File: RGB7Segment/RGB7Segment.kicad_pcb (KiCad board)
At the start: 2 copper layers, 18.3 x 17 mm, 21 parts, among them J1 Conn_01x02_Socket, J2 Conn_01x02_Socket

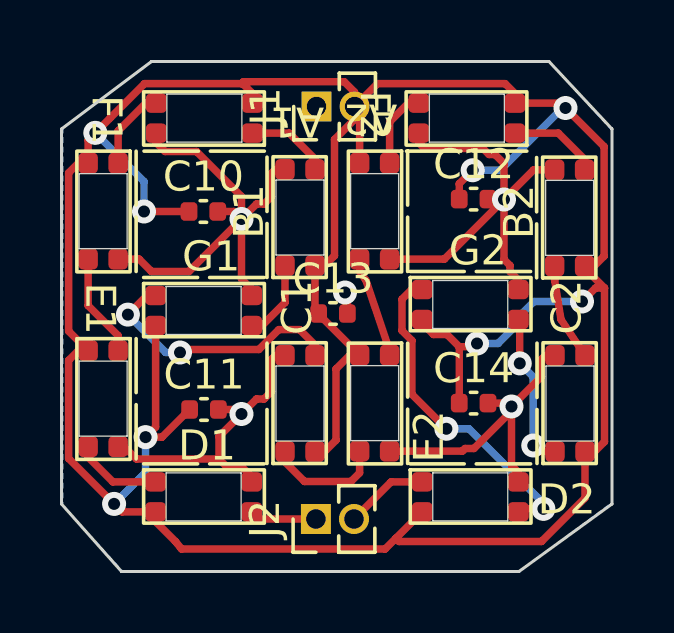
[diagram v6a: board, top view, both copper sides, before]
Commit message: Smaller Footprint, removed all traces, pre-re-layout
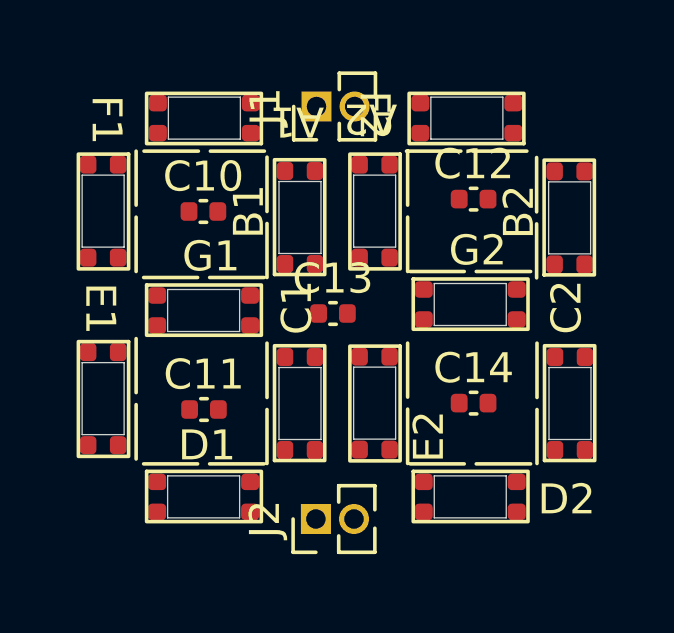
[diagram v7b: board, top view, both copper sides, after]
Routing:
- net VCC: track 109.8 -> 0.50 mm, vias 8 -> 0
- net GND: track 52.9 -> 0.00 mm, vias 5 -> 0
- net Net-(D2-DIN): track 11.1 -> 0.00 mm, vias 2 -> 0
- net Net-(C1-DIN): track 8.83 -> 0.00 mm, vias 2 -> 0
- net Net-(C2-DOUT): track 5.21 -> 0.00 mm, vias 2 -> 0
- net /E2: track 3.95 -> 0.00 mm
- net Net-(E1-DOUT): track 3.46 -> 0.00 mm
- net Net-(E2-DOUT): track 3.42 -> 0.00 mm
- net Net-(B2-DOUT): track 3.25 -> 0.00 mm
- net Net-(A2-DOUT): track 3.04 -> 0.00 mm
- net Net-(D1-DOUT): track 2.94 -> 0.00 mm
- net Net-(A1-DOUT): track 2.79 -> 0.00 mm
- net /DOUT: track 2.79 -> 0.00 mm
- net Net-(A1-DIN): track 2.73 -> 0.00 mm
- net Net-(B1-DOUT): track 2.67 -> 0.00 mm
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- removed copper zone on B.Cu, net GND
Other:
- board size 18.3 x 17 mm -> 1.4 x 2.4 mm

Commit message: New Layout possibility
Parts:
- moved C2 1.28 mm to (208.9, 87.7)
- moved B2 1.27 mm to (208.9, 81.5)
- moved F1 1.12 mm to (194.8, 78.7)
- moved E1 1.11 mm to (194.8, 84.9)
- moved C12 1.00 mm to (205.6, 80.0)
- moved C14 0.65 mm to (205.8, 86.2)
- moved G2 0.60 mm to (204.5, 83.8)
- moved A2 0.56 mm to (207.1, 76.4)
- moved D2 0.56 mm to (204.5, 90.0)
- moved C10 0.45 mm to (197.9, 80.0)
- moved D1 0.45 mm to (196.6, 90.0)
- moved G1 0.45 mm to (196.6, 83.8)
- moved A1 0.45 mm to (199.3, 76.4)
- moved C11 0.45 mm to (197.9, 86.6)
- moved J2 0.35 mm to (201.2, 89.9)
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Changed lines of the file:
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@@
 	(footprint "Library:12-23C"
 		(layer "F.Cu")
-		(at 210.137501 81.5625 90)
+		(at 208.875 81.45 90)
 		(property "Reference" "B2"
-			(at 1.55 -2.137501 90)
+			(at 2.7 -2.0375 90)
 			(unlocked yes)
 			(layer "F.SilkS")
 			(effects
 				(font
-					(size 1 1)
+					(size 0.75 0.75)
 					(thickness 0.15)
 				)
@@
 	(footprint "Library:12-23C"
 		(layer "F.Cu")
-		(at 196.1375 83.75)
+		(at 196.5875 83.75)
 		(property "Reference" "G1"
 			(at 1.6 -2.25 0)
@@
 			(effects
 				(font
-					(size 1 1)
+					(size 0.75 0.75)
 					(thickness 0.15)
 				)
@@
 	(footprint "Library:12-23C"
 		(layer "F.Cu")
-		(at 196.1375 89.9625)
+		(at 196.5875 89.9625)
 		(property "Reference" "D1"
 			(at 1.4625 -2.1625 0)
@@
 			(effects
 				(font
-					(size 1 1)
+					(size 0.75 0.75)
 					(thickness 0.15)
 				)
@@
 	(footprint "Library:12-23C"
 		(layer "F.Cu")
-		(at 207.6125 76.4375 180)
+		(at 207.05 76.4375 180)
 		(property "Reference" "A2"
-			(at 4.575 -0.462499 180)
+			(at -1.1875 -0.4125 90)
 			(unlocked yes)
 			(layer "F.SilkS")
 			(effects
 				(font
-					(size 1 1)
+					(size 0.75 0.75)
 					(thickness 0.15)
 				)
@@
 		(tags "Through hole pin header THT 1x02 1.27mm single row")
 		(property "Reference" "J1"
-			(at 0 -1.695 90)
+			(at -2.05 0.6 -90)
 			(layer "F.SilkS")
 			(effects
 				(font
-					(size 1 1)
-					(thickness 0.15)
+					(size 0.5 0.5)
+					(thickness 0.125)
 				)
 			)
@@
 	(footprint "Capacitor_SMD:C_0402_1005Metric"
 		(layer "F.Cu")
-		(at 206.4875 79.5875)
+		(at 205.6 80.05)
 		(descr "Capacitor SMD 0402 (1005 Metric), square (rectangular) end terminal, IPC_7351 nominal, (Body size source: IPC-SM-782 page 76, https://www.pcb-3d.com/wordpress/wp-content/uploads/ipc-sm-782a_amendment_1_and_2.pdf), generated with kicad-footprint-generator")
 		(tags "capacitor")
 		(property "Reference" "C12"
-			(at 0 -1.16 0)
+			(at -0.25 -0.9 0)
 			(layer "F.SilkS")
 			(effects
 				(font
-					(size 1 1)
+					(size 0.75 0.75)
 					(thickness 0.15)
 				)
@@
 	(footprint "Library:12-23C"
 		(layer "F.Cu")
-		(at 205.025 83.55)
+		(at 204.4625 83.75)
 		(property "Reference" "G2"
 			(at 1.6 -2.25 0)
@@
 			(effects
 				(font
-					(size 1 1)
+					(size 0.75 0.75)
 					(thickness 0.15)
 				)
@@
 	(footprint "Connector_PinHeader_1.27mm:PinHeader_1x02_P1.27mm_Vertical"
 		(layer "F.Cu")
-		(at 201.229999 90.25 90)
+		(at 201.23 89.9 90)
 		(descr "Through hole straight pin header, 1x02, 1.27mm pitch, single row")
 		(tags "Through hole pin header THT 1x02 1.27mm single row")
 		(property "Reference" "J2"
-			(at 0 -1.695 90)
+			(at 2.15 0.72 270)
 			(layer "F.SilkS")
 			(effects
 				(font
-					(size 1 1)
-					(thickness 0.15)
+					(size 0.5 0.5)
+					(thickness 0.125)
 				)
 			)
@@
 		(tags "capacitor")
 		(property "Reference" "C13"
-			(at 0 -1.16 0)
+			(at 0 -0.95 0)
 			(layer "F.SilkS")
 			(effects
 				(font
-					(size 1 1)
+					(size 0.75 0.75)
 					(thickness 0.15)
 				)
@@
 	(footprint "Library:12-23C"
 		(layer "F.Cu")
-		(at 202.7375 78.6375 -90)
+		(at 202.6875 78.75 -90)
 		(property "Reference" "F2"
-			(at -1.8375 -0.45 -90)
+			(at 2.6 -2.15 270)
 			(unlocked yes)
 			(layer "F.SilkS")
 			(effects
 				(font
-					(size 1 1)
+					(size 0.75 0.75)
 					(thickness 0.15)
 				)
@@
 	(footprint "Library:12-23C"
 		(layer "F.Cu")
-		(at 193.6875 84.8875 -90)
+		(at 194.8 84.94375 -90)
 		(property "Reference" "E1"
-			(at -1.65 -0.35 -90)
+			(at -1.65 -0.35 270)
 			(unlocked yes)
 			(layer "F.SilkS")
 			(effects
 				(font
-					(size 1 1)
+					(size 0.75 0.75)
 					(thickness 0.15)
 				)
@@
 	(footprint "Capacitor_SMD:C_0402_1005Metric"
 		(layer "F.Cu")
-		(at 206.4875 86.3875)
+		(at 205.85 86.25)
 		(descr "Capacitor SMD 0402 (1005 Metric), square (rectangular) end terminal, IPC_7351 nominal, (Body size source: IPC-SM-782 page 76, https://www.pcb-3d.com/wordpress/wp-content/uploads/ipc-sm-782a_amendment_1_and_2.pdf), generated with kicad-footprint-generator")
 		(tags "capacitor")
@@
 			(effects
 				(font
-					(size 1 1)
+					(size 0.75 0.75)
 					(thickness 0.15)
 				)
@@
 	(footprint "Capacitor_SMD:C_0402_1005Metric"
 		(layer "F.Cu")
-		(at 197.48 80)
+		(at 197.93 80)
 		(descr "Capacitor SMD 0402 (1005 Metric), square (rectangular) end terminal, IPC_7351 nominal, (Body size source: IPC-SM-782 page 76, https://www.pcb-3d.com/wordpress/wp-content/uploads/ipc-sm-782a_amendment_1_and_2.pdf), generated with kicad-footprint-generator")
 		(tags "capacitor")
@@
 			(effects
 				(font
-					(size 1 1)
+					(size 0.75 0.75)
 					(thickness 0.15)
 				)
@@
 	(footprint "Library:12-23C"
 		(layer "F.Cu")
-		(at 198.8625 76.4375 180)
+		(at 199.3125 76.4375 180)
 		(property "Reference" "A1"
-			(at -1.7375 -0.562501 180)
+			(at 4.1125 -0.4625 0)
 			(unlocked yes)
 			(layer "F.SilkS")
 			(effects
 				(font
-					(size 1 1)
+					(size 0.75 0.75)
 					(thickness 0.15)
 				)
@@
 	(footprint "Library:12-23C"
 		(layer "F.Cu")
-		(at 201.149999 81.55 90)
+		(at 201.0375 81.45 90)
 		(property "Reference" "B1"
 			(at 1.55 -2.149999 90)
@@
 			(effects
 				(font
-					(size 1 1)
+					(size 0.75 0.75)
 					(thickness 0.15)
 				)
@@
 	(footprint "Library:12-23C"
 		(layer "F.Cu")
-		(at 205.025 89.9625)
+		(at 204.4625 89.9625)
 		(property "Reference" "D2"
 			(at 4.5625 -0.3625 0)
@@
 			(effects
 				(font
-					(size 1 1)
+					(size 0.75 0.75)
 					(thickness 0.15)
 				)
@@
 	(footprint "Library:12-23C"
 		(layer "F.Cu")
-		(at 210.15 87.75 90)
+		(at 208.875 87.65625 90)
 		(property "Reference" "C2"
-			(at 4.5625 -0.5625 90)
+			(at 4.45625 -0.375 90)
 			(unlocked yes)
 			(layer "F.SilkS")
 			(effects
 				(font
-					(size 1 1)
+					(size 0.75 0.75)
 					(thickness 0.15)
 				)
@@
 	(footprint "Library:12-23C"
 		(layer "F.Cu")
-		(at 193.6875 78.6375 -90)
+		(at 194.8 78.74375 -90)
 		(property "Reference" "F1"
-			(at -1.6875 -0.5625 -90)
+			(at 2.60625 -2.1 270)
 			(unlocked yes)
 			(layer "F.SilkS")
 			(effects
 				(font
-					(size 1 1)
+					(size 0.75 0.75)
 					(thickness 0.15)
 				)
@@
 	(footprint "Library:12-23C"
 		(layer "F.Cu")
-		(at 202.7375 85.0375 -90)
+		(at 202.8 84.94375 -90)
 		(property "Reference" "E2"
 			(at 2.4625 -2.2625 90)
@@
 			(effects
 				(font
-					(size 1 1)
+					(size 0.75 0.75)
 					(thickness 0.15)
 				)
@@
 	(footprint "Library:12-23C"
 		(layer "F.Cu")
-		(at 201.149999 87.75 90)
+		(at 201.0375 87.65625 90)
 		(property "Reference" "C1"
-			(at 4.55 -0.549999 90)
+			(at 4.05625 -0.3875 90)
 			(unlocked yes)
 			(layer "F.SilkS")
 			(effects
 				(font
-					(size 1 1)
+					(size 0.75 0.75)
 					(thickness 0.15)
 				)
@@
 	(footprint "Capacitor_SMD:C_0402_1005Metric"
 		(layer "F.Cu")
-		(at 197.5 86.6)
+		(at 197.95 86.6)
 		(descr "Capacitor SMD 0402 (1005 Metric), square (rectangular) end terminal, IPC_7351 nominal, (Body size source: IPC-SM-782 page 76, https://www.pcb-3d.com/wordpress/wp-content/uploads/ipc-sm-782a_amendment_1_and_2.pdf), generated with kicad-footprint-generator")
 		(tags "capacitor")
@@
 			(effects
 				(font
-					(size 1 1)
+					(size 0.75 0.75)
 					(thickness 0.15)
 				)
@@
 	)
 	(segment
-		(start 210.187501 81.8125)
-		(end 210.187501 81.887501)
-		(width 0.25)
-		(layer "F.Cu")
-		(net 1)
-	)
-	(segment
-		(start 210.187501 81.8125)
-		(end 210.187501 81.937501)
-		(width 0.25)
-		(layer "F.Cu")
-		(net 1)
-	)
-	(segment
